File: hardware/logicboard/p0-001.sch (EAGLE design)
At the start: 25 parts, among them IC1 74LS07N, IC2 LTC485N, IC3 LTC485N

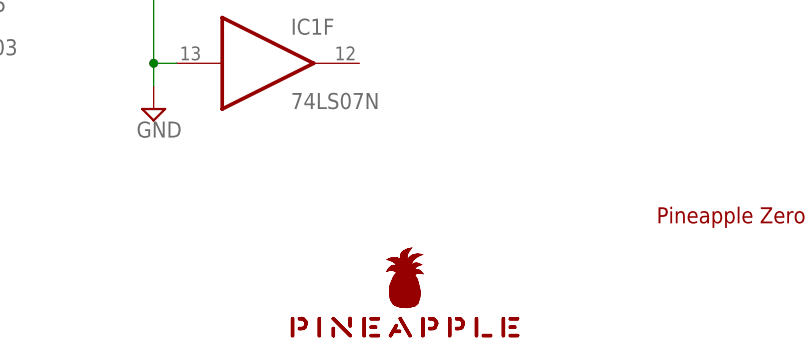
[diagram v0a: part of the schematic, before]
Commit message: Pineapple Logo (vector->bitmap), OSHW logo (silk -> copper).
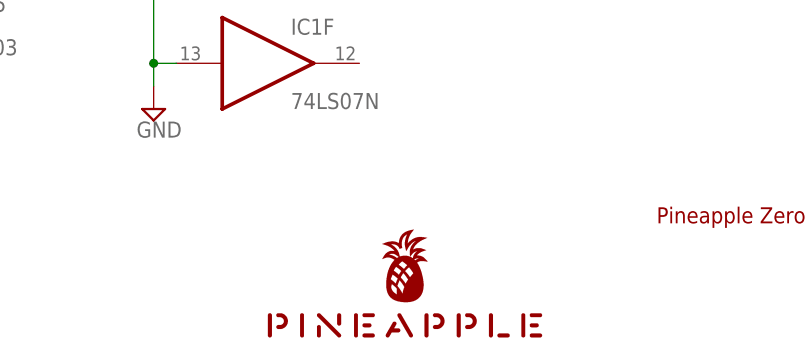
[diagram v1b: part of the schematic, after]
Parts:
- LOGO1: value OSHW-LOGOS -> OSHW-LOGOS-COPPER; device SparkFun-Aesthetics:OSHW-LOGOS -> SparkFun-Aesthetics:OSHW-LOGOS-COPPER
- U$1: value PINEAPPLELOGO2SILKMINI -> PINEAPPLE450; device pineapplelogo:PINEAPPLELOGO2SILKMINI -> pineapple:PINEAPPLE450
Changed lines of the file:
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@@
 <part name="SUPPLY23" library="supply2" library_urn="urn:adsk.eagle:library:372" deviceset="GND" device=""/>
 <part name="FRAME1" library="frames" library_urn="urn:adsk.eagle:library:229" deviceset="A4L-LOC" device=""/>
-<part name="LOGO1" library="SparkFun-Aesthetics" deviceset="OSHW-LOGO" device="S" value="OSHW-LOGOS"/>
-<part name="U$1" library="pineapplelogo" deviceset="PINEAPPLELOGO2SILKMINI" device=""/>
+<part name="LOGO1" library="SparkFun-Aesthetics" deviceset="OSHW-LOGO" device="S-COPPER" value="OSHW-LOGOS-COPPER"/>
+<part name="U$1" library="pineapple" deviceset="PINEAPPLE450" device=""/>
 </parts>
 <sheets>

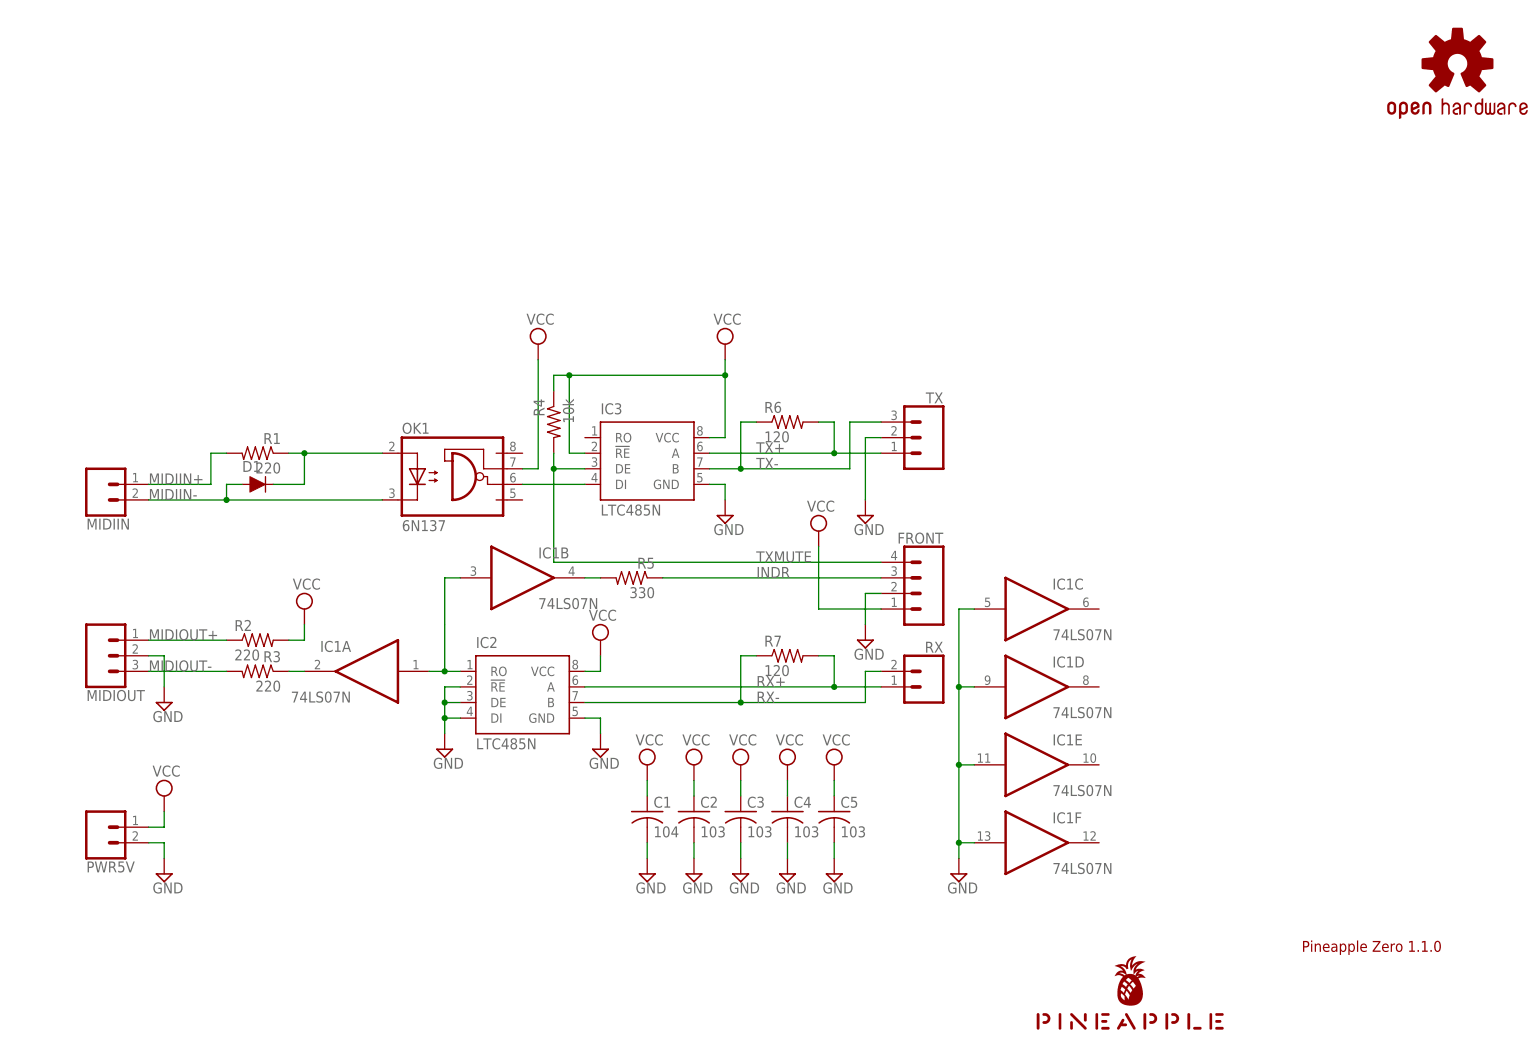
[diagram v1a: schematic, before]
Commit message: Unified MIDI connector.
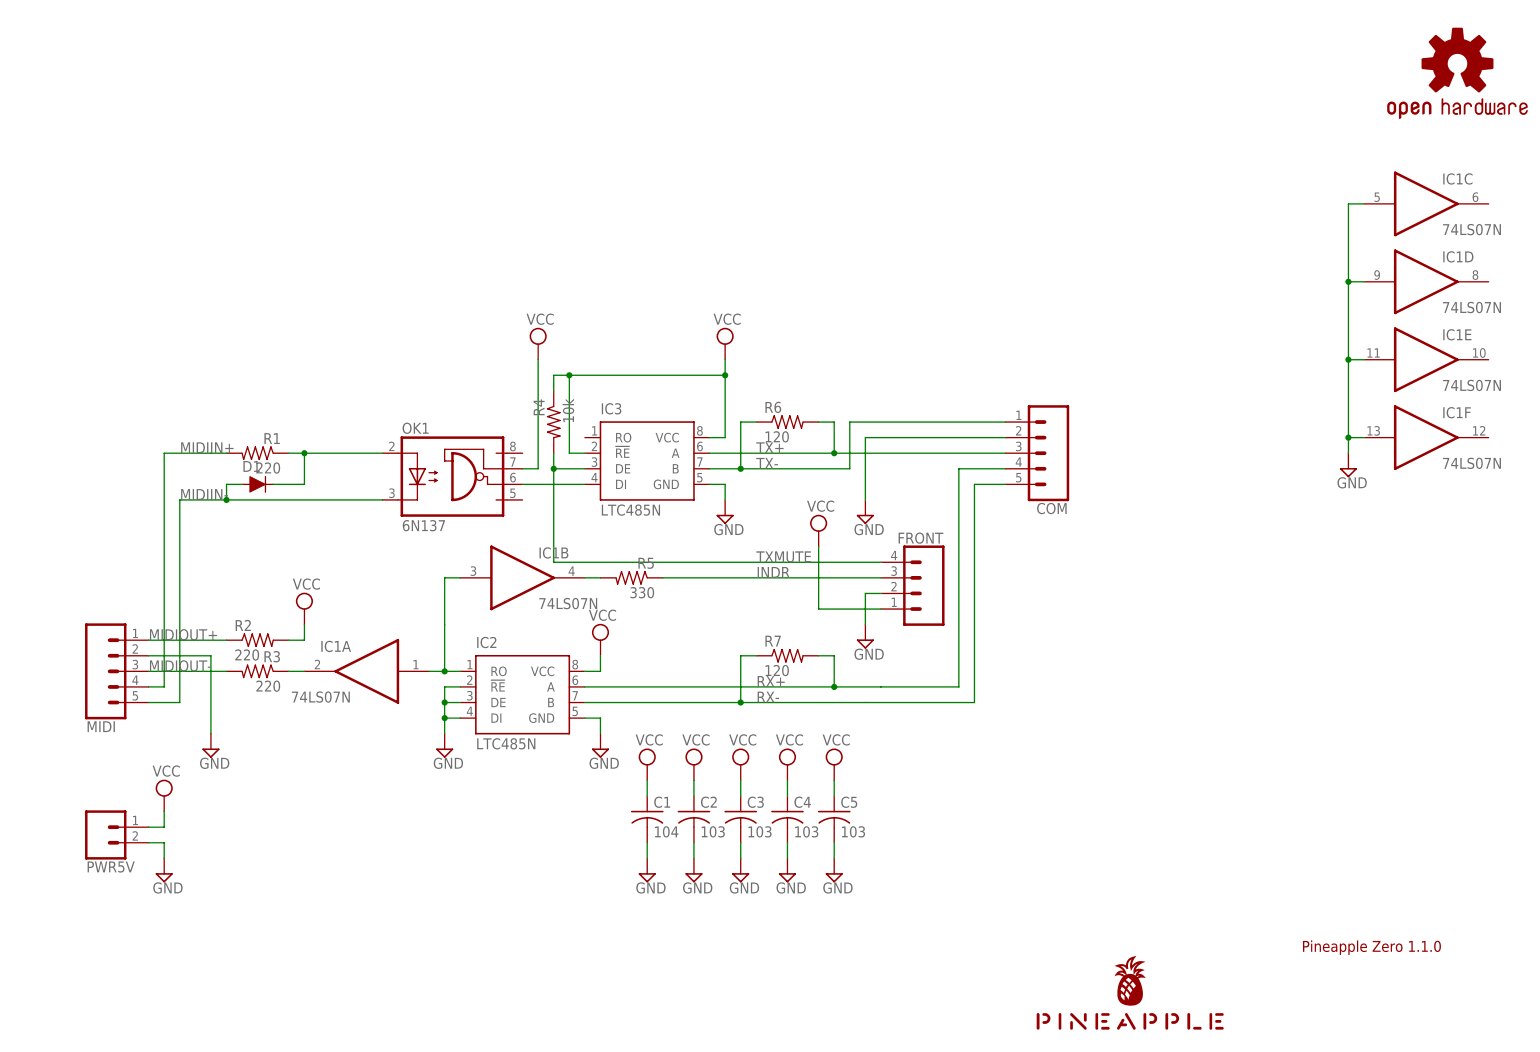
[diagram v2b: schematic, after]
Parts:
- removed MIDIIN, RX: (no value), SparkFun-Connectors:CONN_02JST-PTH-2
- removed MIDIOUT, TX: (no value), SparkFun-Connectors:CONN_03JST-PTH
- added COM, MIDI: (no value), SparkFun-Connectors:CONN_05JST
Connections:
- net GND: now also COM.2, MIDI.2; no longer MIDIOUT.2, TX.2
- net MIDIIN+: now also MIDI.4; no longer MIDIIN.1
- net MIDIIN-: now also MIDI.5; no longer MIDIIN.2
- net MIDIOUT+: now also MIDI.1; no longer MIDIOUT.1
- net MIDIOUT-: now also MIDI.3; no longer MIDIOUT.3
- net RX+: now also COM.4; no longer RX.1
- net RX-: now also COM.5; no longer RX.2
- net TX+: now also COM.3; no longer TX.1
- net TX-: now also COM.1; no longer TX.3
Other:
- moved on the sheet: IC1C, IC1D, IC1E, IC1F
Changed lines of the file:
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@@
 <part name="SUPPLY22" library="supply2" library_urn="urn:adsk.eagle:library:372" deviceset="GND" device=""/>
 <part name="PWR5V" library="SparkFun-Connectors" deviceset="CONN_02" device="JST-PTH-2"/>
-<part name="MIDIIN" library="SparkFun-Connectors" deviceset="CONN_02" device="JST-PTH-2"/>
-<part name="RX" library="SparkFun-Connectors" deviceset="CONN_02" device="JST-PTH-2"/>
-<part name="MIDIOUT" library="SparkFun-Connectors" deviceset="CONN_03" device="JST-PTH"/>
-<part name="TX" library="SparkFun-Connectors" deviceset="CONN_03" device="JST-PTH"/>
 <part name="SUPPLY24" library="supply2" library_urn="urn:adsk.eagle:library:372" deviceset="GND" device=""/>
 <part name="IC1" library="74xx-us" library_urn="urn:adsk.eagle:library:88" deviceset="74*07" device="N" package3d_urn="urn:adsk.eagle:package:2921/1" technology="LS"/>
@@
 <part name="LOGO1" library="SparkFun-Aesthetics" deviceset="OSHW-LOGO" device="S-COPPER" value="OSHW-LOGOS-COPPER"/>
 <part name="U$1" library="pineapple" deviceset="PINEAPPLE450" device=""/>
+<part name="MIDI" library="SparkFun-Connectors" library_urn="urn:adsk.eagle:library:513" deviceset="CONN_05" device="JST" package3d_urn="urn:adsk.eagle:package:38120/1"/>
+<part name="COM" library="SparkFun-Connectors" library_urn="urn:adsk.eagle:library:513" deviceset="CONN_05" device="JST" package3d_urn="urn:adsk.eagle:package:38120/1"/>
 </parts>
 <sheets>
@@
 <instance part="SUPPLY13" gate="G$1" x="121.92" y="119.38"/>
 <instance part="SUPPLY2" gate="G$1" x="30.48" y="45.72"/>
-<instance part="SUPPLY1" gate="GND" x="30.48" y="60.96"/>
+<instance part="SUPPLY1" gate="GND" x="38.1" y="53.34"/>
 <instance part="SUPPLY22" gate="GND" x="144.78" y="91.44"/>
 <instance part="PWR5V" gate="G$1" x="20.32" y="40.64" rot="MR180"/>
-<instance part="MIDIIN" gate="G$1" x="20.32" y="96.52" rot="MR180"/>
-<instance part="RX" gate="G$1" x="154.94" y="63.5" rot="MR0"/>
-<instance part="MIDIOUT" gate="J$1" x="20.32" y="68.58" rot="MR180"/>
-<instance part="TX" gate="J$1" x="154.94" y="104.14" rot="MR0"/>
-<instance part="SUPPLY24" gate="GND" x="160.02" y="33.02"/>
+<instance part="SUPPLY24" gate="GND" x="223.52" y="99.06"/>
 <instance part="IC1" gate="A" x="63.5" y="66.04" rot="MR0"/>
 <instance part="IC1" gate="B" x="88.9" y="81.28"/>
-<instance part="IC1" gate="C" x="172.72" y="76.2"/>
-<instance part="IC1" gate="D" x="172.72" y="63.5"/>
-<instance part="IC1" gate="E" x="172.72" y="50.8"/>
-<instance part="IC1" gate="F" x="172.72" y="38.1"/>
+<instance part="IC1" gate="C" x="236.22" y="142.24"/>
+<instance part="IC1" gate="D" x="236.22" y="129.54"/>
+<instance part="IC1" gate="E" x="236.22" y="116.84"/>
+<instance part="IC1" gate="F" x="236.22" y="104.14"/>
 <instance part="FRONT" gate="G$1" x="152.4" y="78.74" rot="MR0"/>
 <instance part="R5" gate="G$1" x="106.68" y="81.28" rot="MR0"/>
@@
 <instance part="LOGO1" gate="G$1" x="241.3" y="165.1"/>
 <instance part="U$1" gate="G$1" x="187.96" y="7.62"/>
+<instance part="MIDI" gate="G$1" x="20.32" y="66.04" rot="MR180"/>
+<instance part="COM" gate="G$1" x="175.26" y="101.6" rot="R180"/>
 </instances>
 <busses>
@@
 <segment>
 <pinref part="SUPPLY1" gate="GND" pin="GND"/>
-<wire x1="27.94" y1="68.58" x2="30.48" y2="68.58" width="0.1524" layer="91"/>
-<wire x1="30.48" y1="68.58" x2="30.48" y2="63.5" width="0.1524" layer="91"/>
-<pinref part="MIDIOUT" gate="J$1" pin="2"/>
-</segment>
-<segment>
-<wire x1="147.32" y1="104.14" x2="144.78" y2="104.14" width="0.1524" layer="91"/>
+<wire x1="27.94" y1="68.58" x2="38.1" y2="68.58" width="0.1524" layer="91"/>
+<wire x1="38.1" y1="68.58" x2="38.1" y2="55.88" width="0.1524" layer="91"/>
+<pinref part="MIDI" gate="G$1" pin="2"/>
+</segment>
+<segment>
+<wire x1="167.64" y1="104.14" x2="144.78" y2="104.14" width="0.1524" layer="91"/>
 <pinref part="SUPPLY22" gate="GND" pin="GND"/>
 <wire x1="144.78" y1="104.14" x2="144.78" y2="93.98" width="0.1524" layer="91"/>
-<pinref part="TX" gate="J$1" pin="2"/>
+<pinref part="COM" gate="G$1" pin="2"/>
 </segment>
 <segment>
@@
 <segment>
 <pinref part="IC1" gate="C" pin="I"/>
-<wire x1="162.56" y1="76.2" x2="160.02" y2="76.2" width="0.1524" layer="91"/>
+<wire x1="226.06" y1="142.24" x2="223.52" y2="142.24" width="0.1524" layer="91"/>
 <pinref part="SUPPLY24" gate="GND" pin="GND"/>
-<wire x1="160.02" y1="76.2" x2="160.02" y2="63.5" width="0.1524" layer="91"/>
+<wire x1="223.52" y1="142.24" x2="223.52" y2="129.54" width="0.1524" layer="91"/>
 <pinref part="IC1" gate="F" pin="I"/>
-<wire x1="160.02" y1="63.5" x2="160.02" y2="50.8" width="0.1524" layer="91"/>
-<wire x1="160.02" y1="50.8" x2="160.02" y2="38.1" width="0.1524" layer="91"/>
-<wire x1="160.02" y1="38.1" x2="160.02" y2="35.56" width="0.1524" layer="91"/>
-<wire x1="162.56" y1="38.1" x2="160.02" y2="38.1" width="0.1524" layer="91"/>
-<junction x="160.02" y="38.1"/>
+<wire x1="223.52" y1="129.54" x2="223.52" y2="116.84" width="0.1524" layer="91"/>
+<wire x1="223.52" y1="116.84" x2="223.52" y2="104.14" width="0.1524" layer="91"/>
+<wire x1="223.52" y1="104.14" x2="223.52" y2="101.6" width="0.1524" layer="91"/>
+<wire x1="226.06" y1="104.14" x2="223.52" y2="104.14" width="0.1524" layer="91"/>
+<junction x="223.52" y="104.14"/>
 <pinref part="IC1" gate="E" pin="I"/>
-<wire x1="162.56" y1="50.8" x2="160.02" y2="50.8" width="0.1524" layer="91"/>
-<junction x="160.02" y="50.8"/>
+<wire x1="226.06" y1="116.84" x2="223.52" y2="116.84" width="0.1524" layer="91"/>
+<junction x="223.52" y="116.84"/>
 <pinref part="IC1" gate="D" pin="I"/>
-<wire x1="162.56" y1="63.5" x2="160.02" y2="63.5" width="0.1524" layer="91"/>
-<junction x="160.02" y="63.5"/>
+<wire x1="226.06" y1="129.54" x2="223.52" y2="129.54" width="0.1524" layer="91"/>
+<junction x="223.52" y="129.54"/>
 </segment>
 </net>
@@
 <wire x1="139.7" y1="106.68" x2="139.7" y2="101.6" width="0.1524" layer="91"/>
 <label x="127" y="101.6" size="1.778" layer="95"/>
-<wire x1="147.32" y1="101.6" x2="139.7" y2="101.6" width="0.1524" layer="91"/>
+<wire x1="167.64" y1="101.6" x2="139.7" y2="101.6" width="0.1524" layer="91"/>
 <junction x="139.7" y="101.6"/>
-<pinref part="TX" gate="J$1" pin="1"/>
+<pinref part="COM" gate="G$1" pin="3"/>
 </segment>
 </net>
@@
 <wire x1="40.64" y1="93.98" x2="40.64" y2="96.52" width="0.1524" layer="91"/>
 <wire x1="40.64" y1="96.52" x2="43.18" y2="96.52" width="0.1524" layer="91"/>
-<label x="27.94" y="93.98" size="1.778" layer="95"/>
-<wire x1="40.64" y1="93.98" x2="27.94" y2="93.98" width="0.1524" layer="91"/>
+<label x="33.02" y="93.98" size="1.778" layer="95"/>
 <pinref part="OK1" gate="A" pin="C"/>
 <wire x1="66.04" y1="93.98" x2="40.64" y2="93.98" width="0.1524" layer="91"/>
+<pinref part="MIDI" gate="G$1" pin="5"/>
+<wire x1="27.94" y1="60.96" x2="33.02" y2="60.96" width="0.1524" layer="91"/>
+<wire x1="33.02" y1="60.96" x2="33.02" y2="93.98" width="0.1524" layer="91"/>
+<wire x1="33.02" y1="93.98" x2="40.64" y2="93.98" width="0.1524" layer="91"/>
 <junction x="40.64" y="93.98"/>
-<pinref part="MIDIIN" gate="G$1" pin="2"/>
 </segment>
 </net>
@@
 <wire x1="139.7" y1="63.5" x2="147.32" y2="63.5" width="0.1524" layer="91"/>
 <junction x="139.7" y="63.5"/>
-<pinref part="RX" gate="G$1" pin="1"/>
+<pinref part="COM" gate="G$1" pin="4"/>
+<wire x1="167.64" y1="99.06" x2="160.02" y2="99.06" width="0.1524" layer="91"/>
+<wire x1="160.02" y1="99.06" x2="160.02" y2="63.5" width="0.1524" layer="91"/>
+<wire x1="160.02" y1="63.5" x2="147.32" y2="63.5" width="0.1524" layer="91"/>
 </segment>
 </net>
@@
 <wire x1="124.46" y1="60.96" x2="99.06" y2="60.96" width="0.1524" layer="91"/>
 <label x="127" y="60.96" size="1.778" layer="95"/>
-<wire x1="147.32" y1="66.04" x2="144.78" y2="66.04" width="0.1524" layer="91"/>
-<wire x1="144.78" y1="66.04" x2="144.78" y2="60.96" width="0.1524" layer="91"/>
 <wire x1="144.78" y1="60.96" x2="124.46" y2="60.96" width="0.1524" layer="91"/>
 <junction x="124.46" y="60.96"/>
-<pinref part="RX" gate="G$1" pin="2"/>
+<pinref part="COM" gate="G$1" pin="5"/>
+<wire x1="167.64" y1="96.52" x2="162.56" y2="96.52" width="0.1524" layer="91"/>
+<wire x1="162.56" y1="96.52" x2="162.56" y2="60.96" width="0.1524" layer="91"/>
+<wire x1="162.56" y1="60.96" x2="144.78" y2="60.96" width="0.1524" layer="91"/>
 </segment>
 </net>
@@
 <junction x="124.46" y="99.06"/>
 <label x="127" y="99.06" size="1.778" layer="95"/>
-<wire x1="147.32" y1="106.68" x2="142.24" y2="106.68" width="0.1524" layer="91"/>
+<wire x1="167.64" y1="106.68" x2="142.24" y2="106.68" width="0.1524" layer="91"/>
 <wire x1="142.24" y1="106.68" x2="142.24" y2="99.06" width="0.1524" layer="91"/>
-<pinref part="TX" gate="J$1" pin="3"/>
+<pinref part="COM" gate="G$1" pin="1"/>
 </segment>
 </net>
@@
 <pinref part="R1" gate="G$1" pin="2"/>
 <wire x1="40.64" y1="101.6" x2="38.1" y2="101.6" width="0.1524" layer="91"/>
-<label x="27.94" y="96.52" size="1.778" layer="95"/>
-<wire x1="38.1" y1="101.6" x2="38.1" y2="96.52" width="0.1524" layer="91"/>
-<wire x1="38.1" y1="96.52" x2="27.94" y2="96.52" width="0.1524" layer="91"/>
-<pinref part="MIDIIN" gate="G$1" pin="1"/>
+<label x="33.02" y="101.6" size="1.778" layer="95"/>
+<pinref part="MIDI" gate="G$1" pin="4"/>
+<wire x1="27.94" y1="63.5" x2="30.48" y2="63.5" width="0.1524" layer="91"/>
+<wire x1="30.48" y1="63.5" x2="30.48" y2="101.6" width="0.1524" layer="91"/>
+<wire x1="30.48" y1="101.6" x2="38.1" y2="101.6" width="0.1524" layer="91"/>
 </segment>
 </net>
@@
 <wire x1="27.94" y1="66.04" x2="40.64" y2="66.04" width="0.1524" layer="91"/>
 <label x="27.94" y="66.04" size="1.778" layer="95"/>
-<pinref part="MIDIOUT" gate="J$1" pin="3"/>
+<pinref part="MIDI" gate="G$1" pin="3"/>
 </segment>
 </net>
@@
 <wire x1="27.94" y1="71.12" x2="40.64" y2="71.12" width="0.1524" layer="91"/>
 <label x="27.94" y="71.12" size="1.778" layer="95"/>
-<pinref part="MIDIOUT" gate="J$1" pin="1"/>
-</segment>
-</net>
+<pinref part="MIDI" gate="G$1" pin="1"/>
+</segment>
+</net>
